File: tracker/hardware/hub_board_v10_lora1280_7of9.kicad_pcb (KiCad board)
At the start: 4 copper layers, 72 x 80 mm, 49 parts, among them U1 U1, U2 U2, U3 U3, U5 U5, U6 U6, U7 U7

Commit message: feat(router): route the remaining board nets -- 2 clean, 9 blocked by edge connectors
Operator: "some of the things on this board look straight forward to route, please do those before
asking me to take over." Enumerated all 46 non-plane nets and routed them with the same corrected
model (per-net ownership, board-derived via sizing, zone refill).

RESULT: 2 nets routed, ZERO new DRC violations, unconnected items 90 -> 86.

  /F33_VCC      span  6.6 mm   routed
  /F33_RESET_N  span 23.7 mm   routed

WHAT THE "STRAIGHTFORWARD" NETS ACTUALLY ARE -- and this is the finding that matters
9 of the short-span nets terminate at edge connectors (J_W1..J_W4, J_HUB_PV). Their pads sit
0.00-0.43 mm from the outline, i.e. THEY ALREADY VIOLATE the 0.5 mm board-edge rule. That is part of
the 16 pre-existing copper_edge_clearance violations, not something this router introduced.

Routing away from such a pad can only add edge violations. Measured, twice:
  * routing all 5 CUT_SENSE_* nets -> +7 copper_edge_clearance (16 -> 23). REJECTED, not shipped.
  * routing W1_SOLAR_P          -> +1 (16 -> 17), still +1 with the keep-out raised to 1.6 mm.
  * refilling zones on the untouched board -> +0, so the pour is not the cause.

Excluded: /CUT_SENSE_W1..W4, /VSCAP, /W1_SOLAR_N, /W1_SOLAR_P, /W2_SOLAR_N, /W3_SOLAR_N -- any net
with a pad within 1.2 mm of the board bounding box. Shoving copper inward would leave the pad itself
still in violation, so the fix is connector placement or the edge rule, and that is a design
decision, not a router parameter.

NEW TOOLING
  tracker/hardware/route_board_nets.py
      Net selection is driven by the DRC, not by guessing: the set is whatever kicad-cli reports as
      unconnected, minus planes (GND/+3V3, which join through the pour). Shortest span first.
      Pads chained for multi-pad nets. Edge-connector nets excluded and REPORTED, never silently.

  route_lora1280_independent.py
      EDGE_KEEP is now REDGE=<mm> (default 0.60, unchanged). Needed be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
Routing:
- net /F33_RESET_N: track 0.00 -> 76.9 mm, vias 0 -> 2
- net /F33_VCC: track 0.00 -> 17.9 mm, vias 0 -> 1

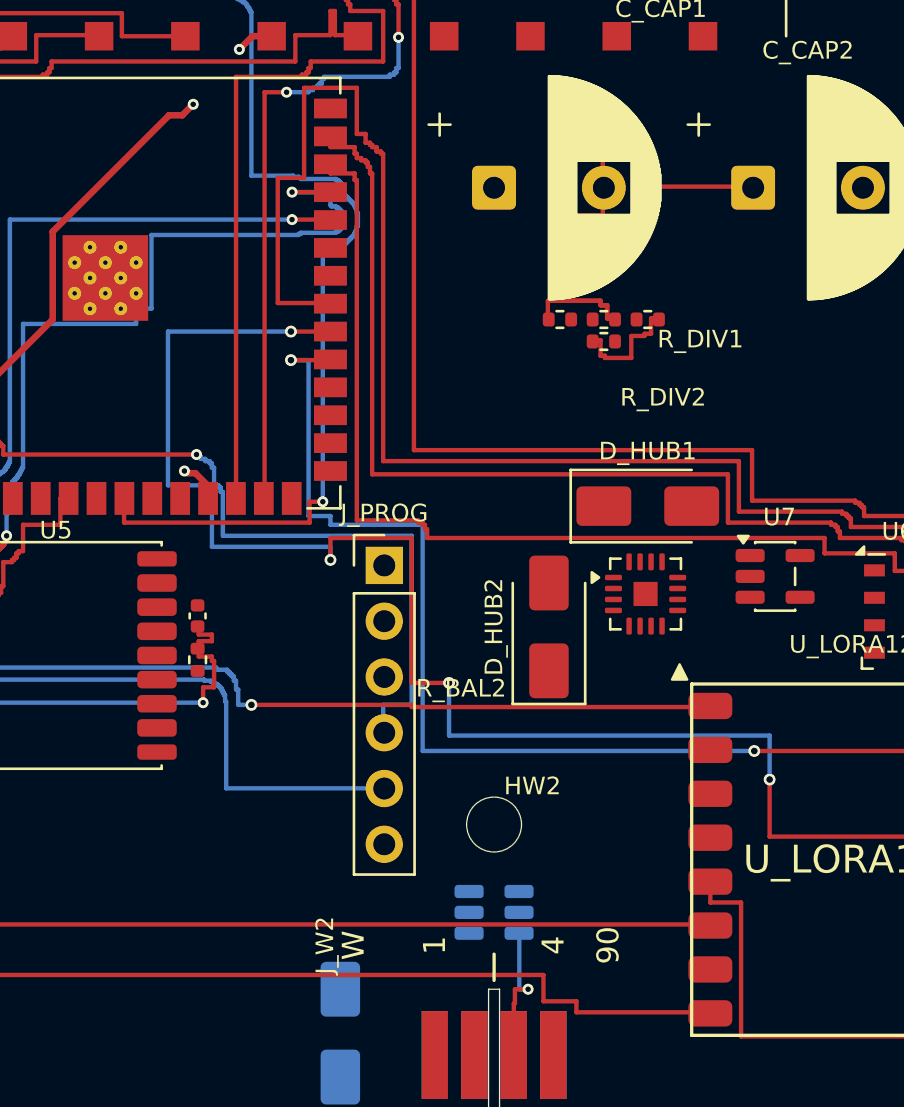
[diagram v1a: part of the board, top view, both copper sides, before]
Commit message: feat(hub): operator's hand-routing of SPI1_SCK and E28_DIO3, folded onto current master
Operator routed both remaining LoRa1280 interface nets by hand in KiCad on the T14, moving several
existing lanes to open the corridors. That work is preserved verbatim here (commit c51c1e45 on
c03rad0r/balloon-fresh-1) with two things added because his base predated them:

  1. F33_VCC and F33_RESET_N re-routed on top, so merging this does not silently delete the two
     nets that landed in bd96d565 after he branched.
  2. Zones refilled. His saved board carried a STALE pour, which read as 136 violations with 46
     clearance. After the refill: 79 violations, 5 clearance. Those 46 were not routing errors --
     they were the old GND pour still sitting where his new tracks now run.

STATE OF THIS BRANCH -- deliberately NOT clean enough to merge:
  LoRa1280 interface   9/9 routed (no unconnected item names SPI1_SCK or E28_DIO3)
  violations           79
  clearance             5   <- REAL, see below
  shorting_items        0
  solder_mask_bridge    0

The five clearance violations, all between 0.149 and 0.161 mm against a 0.200 mm rule:
  * Track /E28_RESET_N (B.Cu) vs segment /SPI1_SCK (B.Cu)  -- 0.1487 mm, twice
  * Segment /SPI1_SCK (F.Cu) vs Pad 21 /F33_VSENSE of U1   -- 0.1533 mm
  * Segment /I2C_SDA (F.Cu) vs segment /I2C_SCL (F.Cu)     -- 0.1606 mm, twice
Each needs about 0.05 mm of breathing room. They are NOT relaxed away: the board rule stays 0.20.
Hand-routes cannot be nudged by the maze router without destroying the operator's work, so these go
back to him with the exact locations.

Also present: Pad 14 [GND] of U_LORA1280 reports "missing connection" to zone GND_FCu. Introduced by
the refill on this board, not by his routing; it is a thermal-spoke question for the next pass.

.gitignore now covers fp-info-cache, *.lck and ~*.kicad_pcb.lck -- KiCad writes both constantly and
they were showing up in the operator's git status.

The .kicad_pro is included: 284 lines, z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
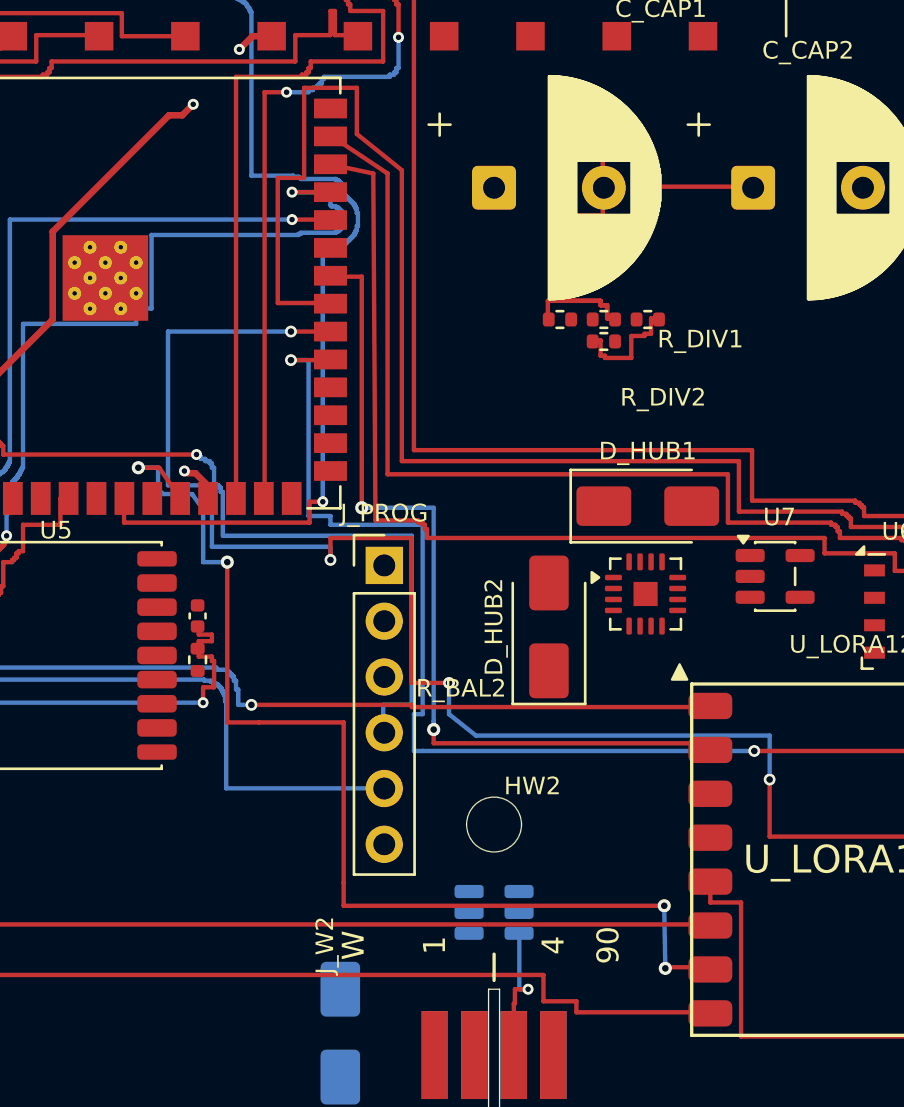
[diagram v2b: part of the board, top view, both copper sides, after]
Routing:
- net /I2C_SCL: track 45.4 -> 27.2 mm
- net /E28_RESET_N: track 71.4 -> 54.4 mm
- net /E28_DIO1: track 74.4 -> 57.4 mm
- net /E28_BUSY: track 53.0 -> 42.7 mm
- net /I2C_SDA: track 49.7 -> 45.4 mm
- net /SPI1_SCK: vias 0 -> 4
- net /E28_DIO3: vias 0 -> 2
